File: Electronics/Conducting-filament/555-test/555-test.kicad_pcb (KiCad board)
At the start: 2 copper layers, 29 x 30 mm, 7 parts, among them J1 Conn_01x02_Male, J2 Conn_01x01_Male, U1 LM555

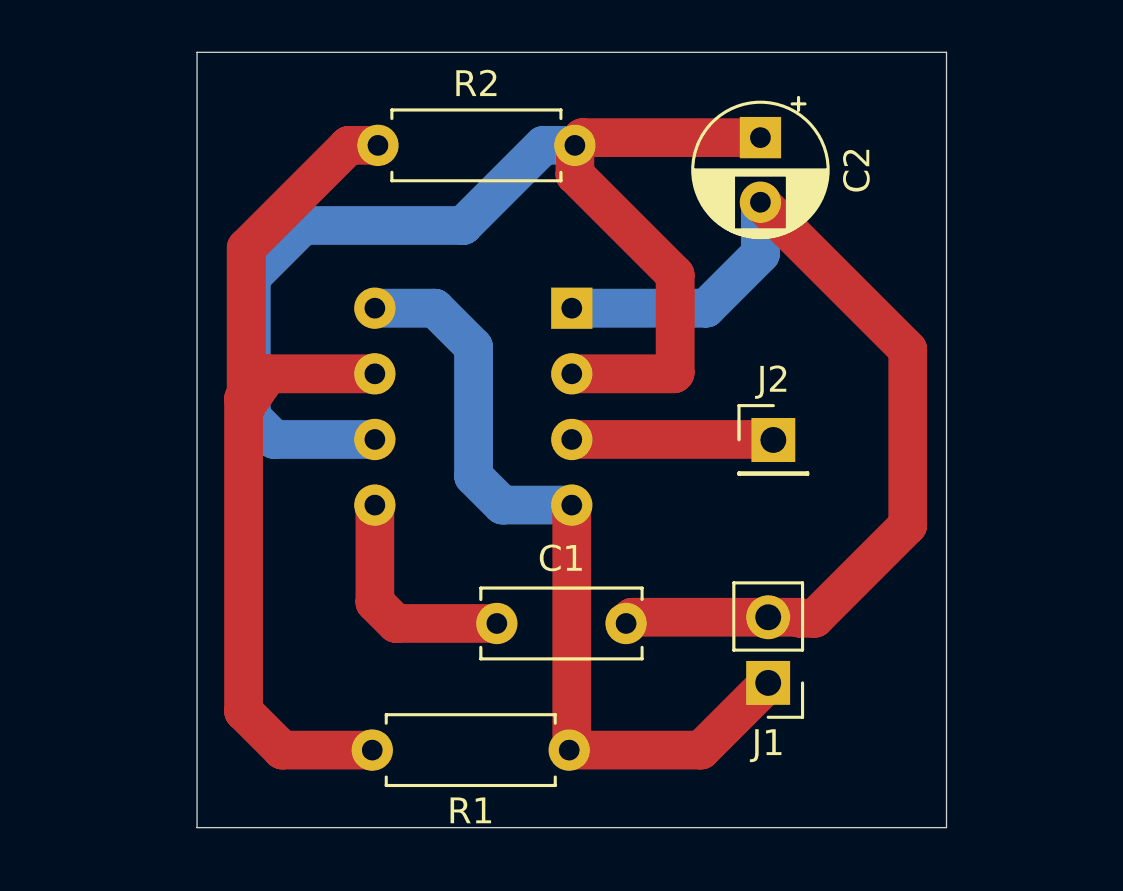
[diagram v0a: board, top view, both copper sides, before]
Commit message: First attempt (not wholly successful) at laying down multiple tracks...
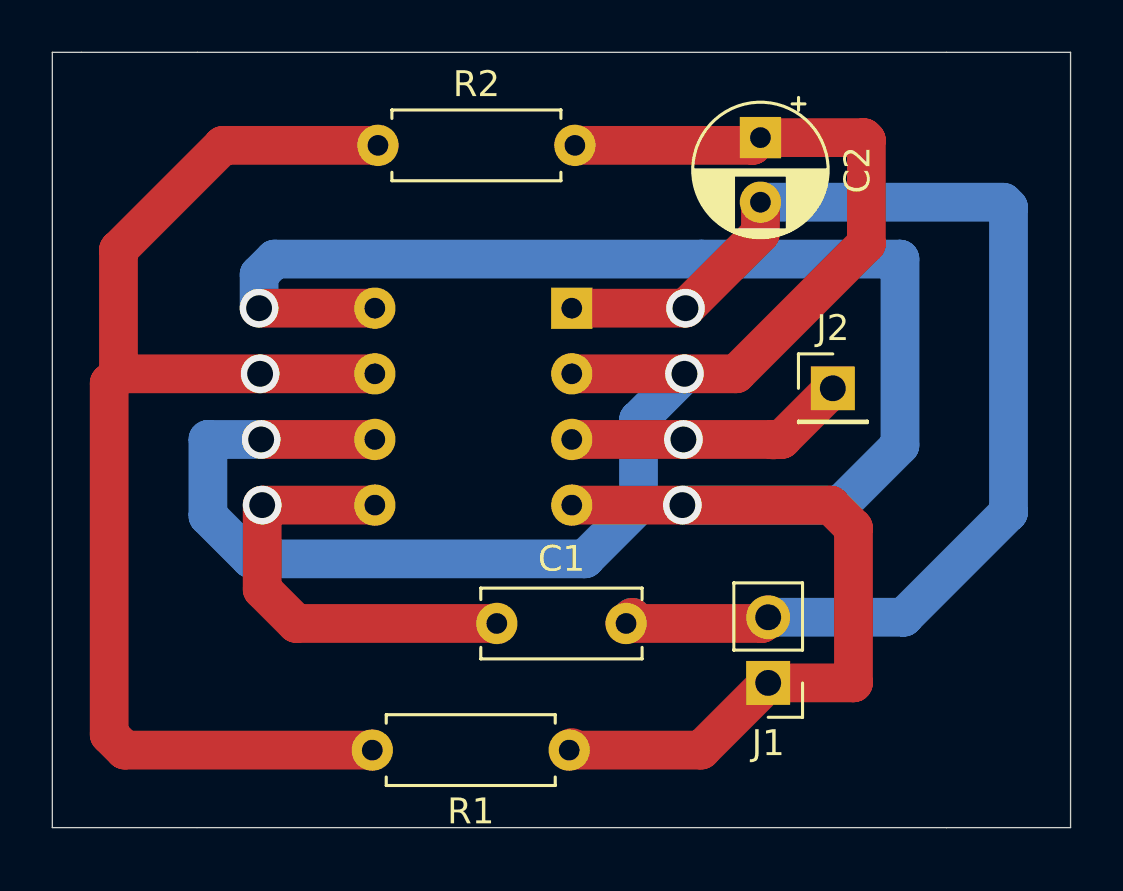
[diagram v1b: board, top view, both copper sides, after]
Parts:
- moved J2 3.05 mm to (24.2, -17.4)
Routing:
- net +5V: track 32.0 -> 76.9 mm, vias 0 -> 2
- net Net-(C2-Pad1): track 46.9 -> 62.4 mm, vias 0 -> 2
- net Net-(R1-Pad2): track 36.5 -> 51.0 mm, vias 0 -> 1
- net GND: track 37.9 -> 48.4 mm, vias 0 -> 1
- net Net-(C1-Pad1): track 8.82 -> 17.2 mm, vias 0 -> 1
- net Net-(J2-Pad1): track 7.81 -> 10.9 mm, vias 0 -> 1
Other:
- board size 29 x 30 mm -> 39.4 x 30 mm

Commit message: Further work on test circuit.
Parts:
- removed J2: Conn_01x01_Male, Connector_PinHeader_2.54mm:PinHeader_1x01_P2.54mm_Vertical
- added D1: LED, LED_THT:LED_D3.0mm, F.Cu at (28.3, -6.30)
- added R3: 220R, Resistor_THT:R_Axial_DIN0207_L6.3mm_D2.5mm_P7.62mm_Horizontal, F.Cu at (28.2, -9.80)
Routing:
- net GND: track 48.4 -> 36.4 mm
- net +5V: track 76.9 -> 67.7 mm
- net Net-(R3-Pad2): track 10.9 -> 15.0 mm
- net Net-(D1-Pad1): track 0.00 -> 3.54 mm
- net Net-(C2-Pad1): track 62.4 -> 65.6 mm
